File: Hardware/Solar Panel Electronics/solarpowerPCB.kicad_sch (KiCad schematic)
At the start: 41 parts, among them J3 Conn_01x02_Male, J4 Conn_01x06_Male, J5 Conn_01x02_Male, Q1 MMDT2222A, U1 SN65HVD230, U2 ESP32-PICO-D4

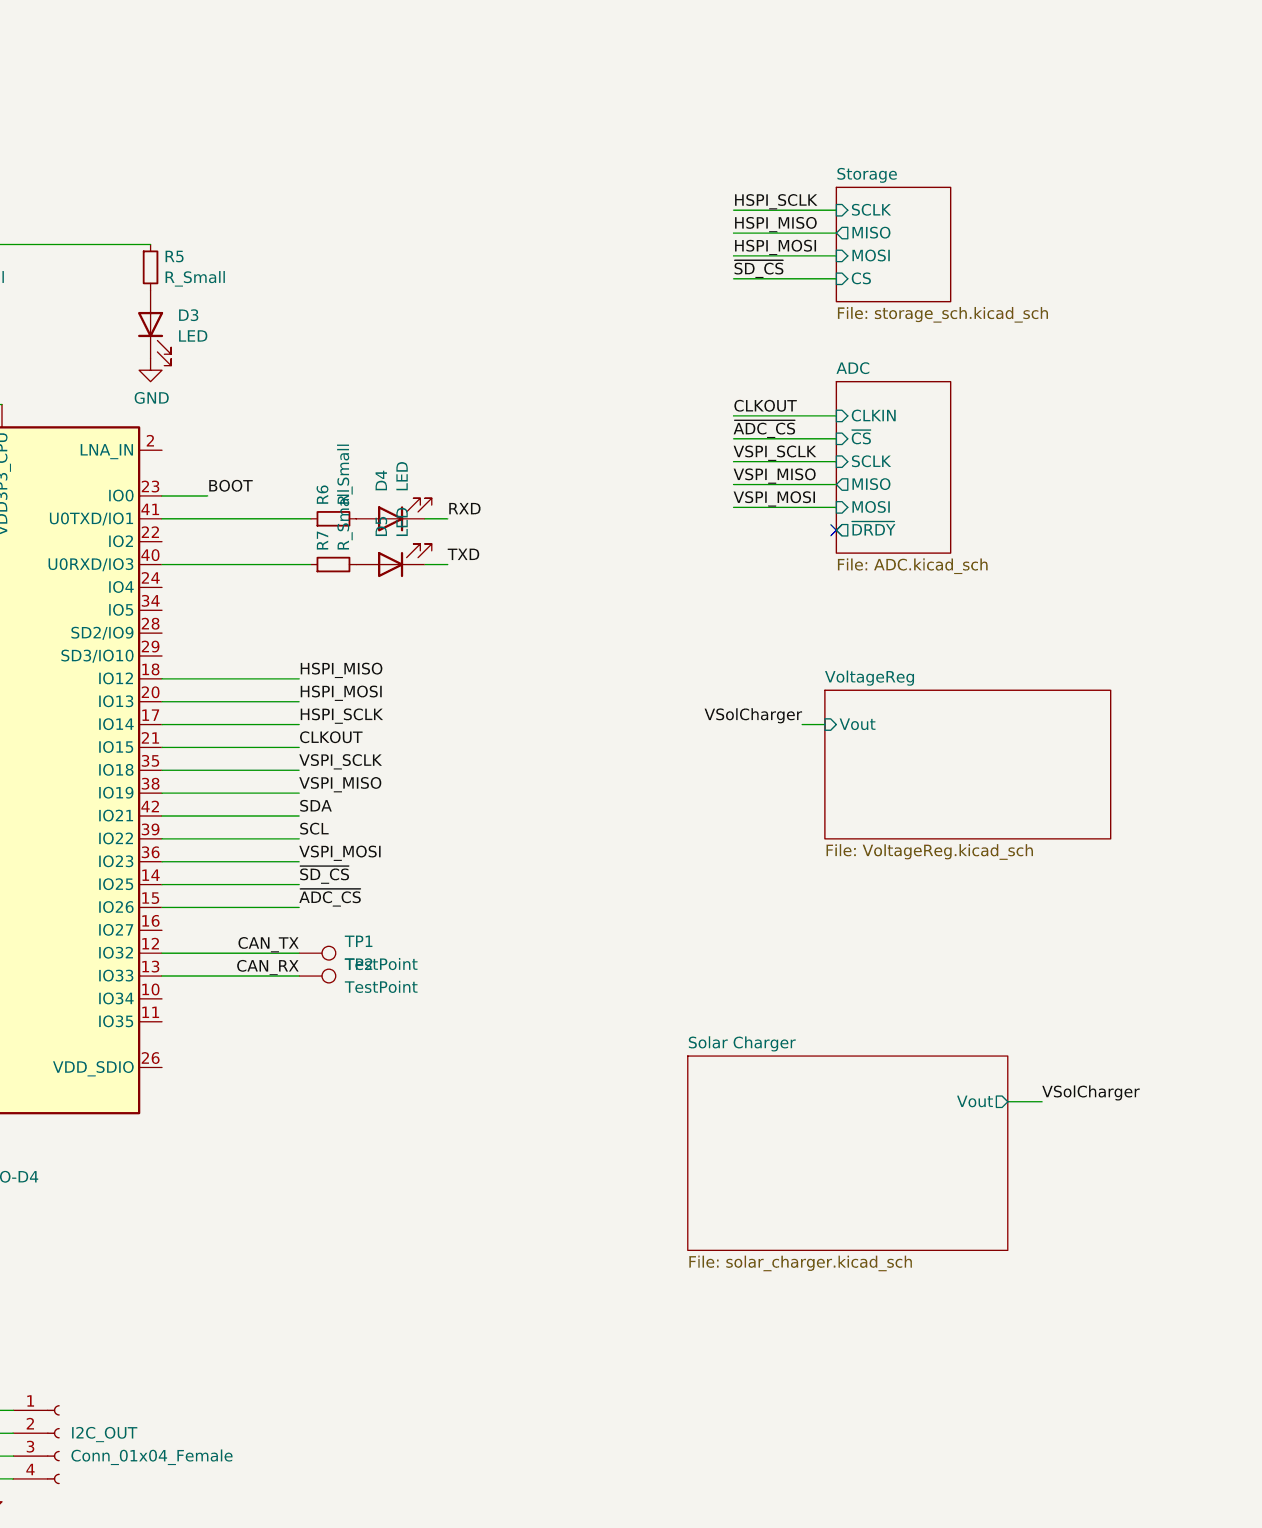
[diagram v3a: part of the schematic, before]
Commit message: Added power measuring circuitry using potential dividers. Needs to be double checked
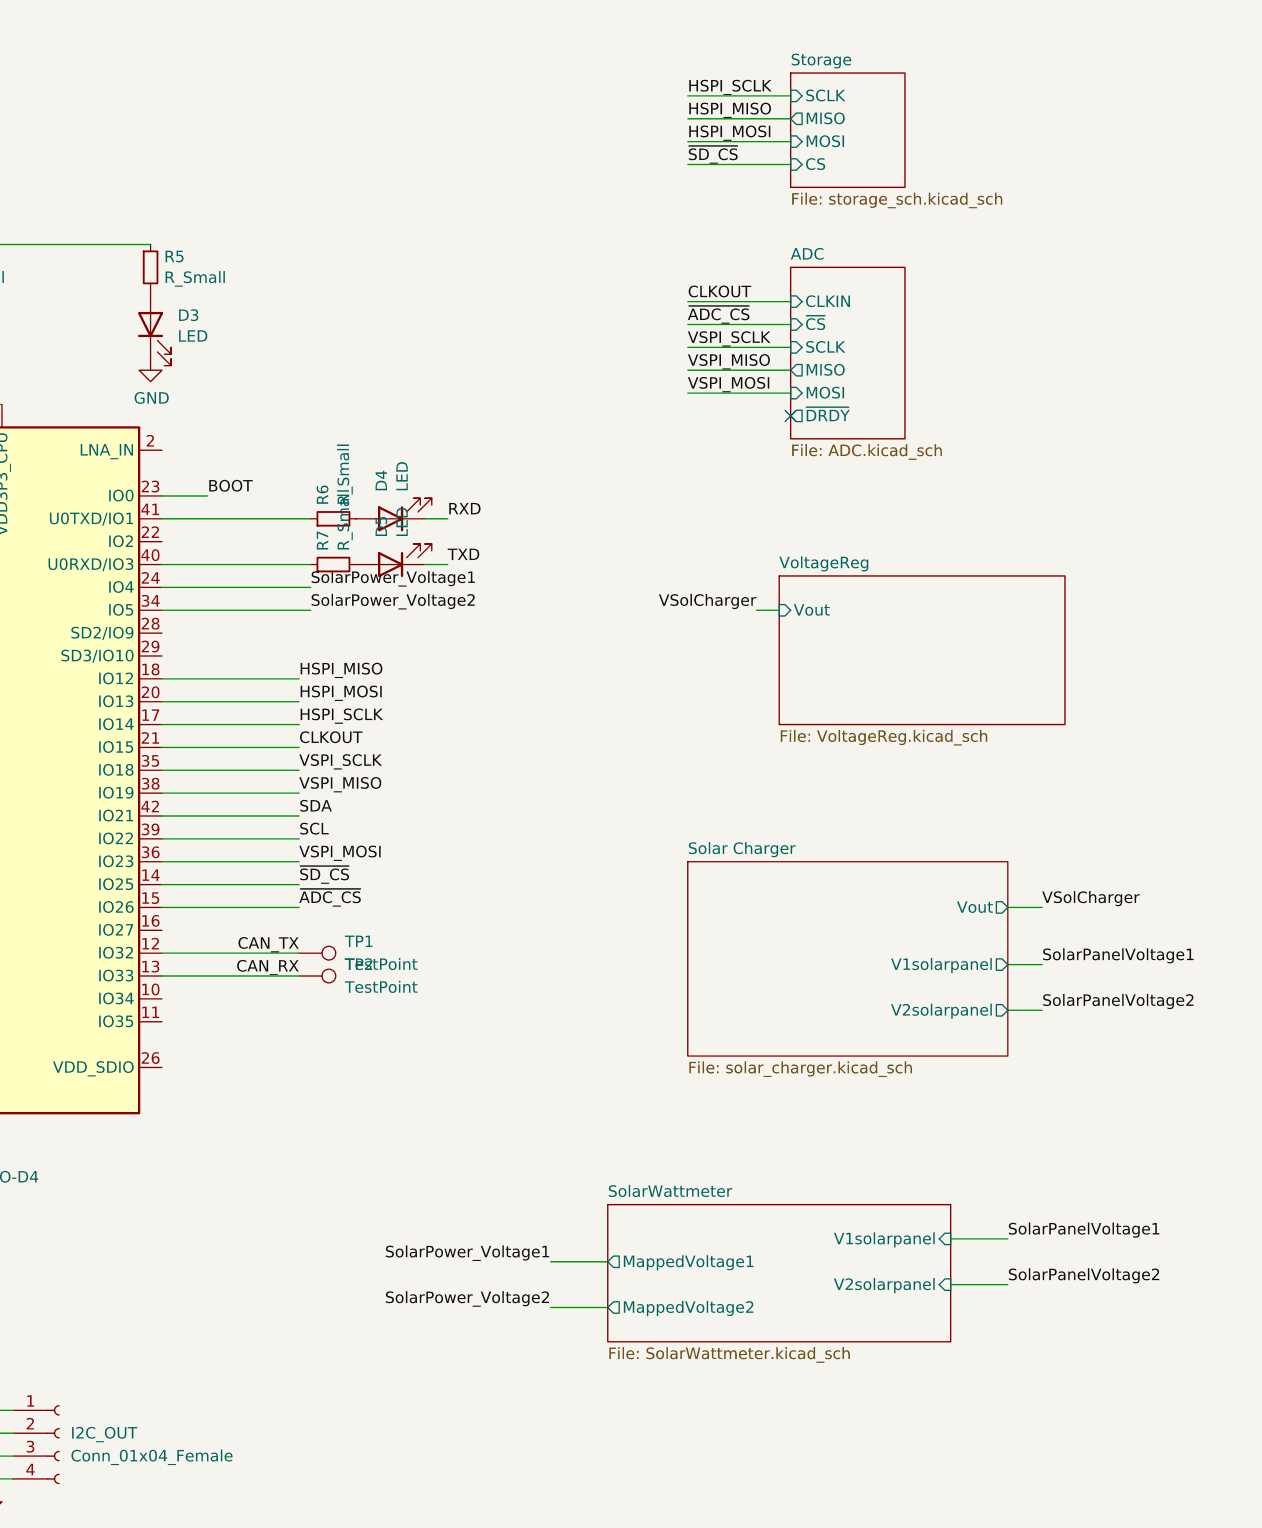
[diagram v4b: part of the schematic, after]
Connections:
- net SolarPower_Voltage1: now reaches U2.24 (IO4)
- net SolarPower_Voltage2: now reaches U2.34 (IO5)
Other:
- added sheet SolarWattmeter (SolarWattmeter.kicad_sch)
- sheet Solar Charger ports: added V1solarpanel, V2solarpanel; removed none

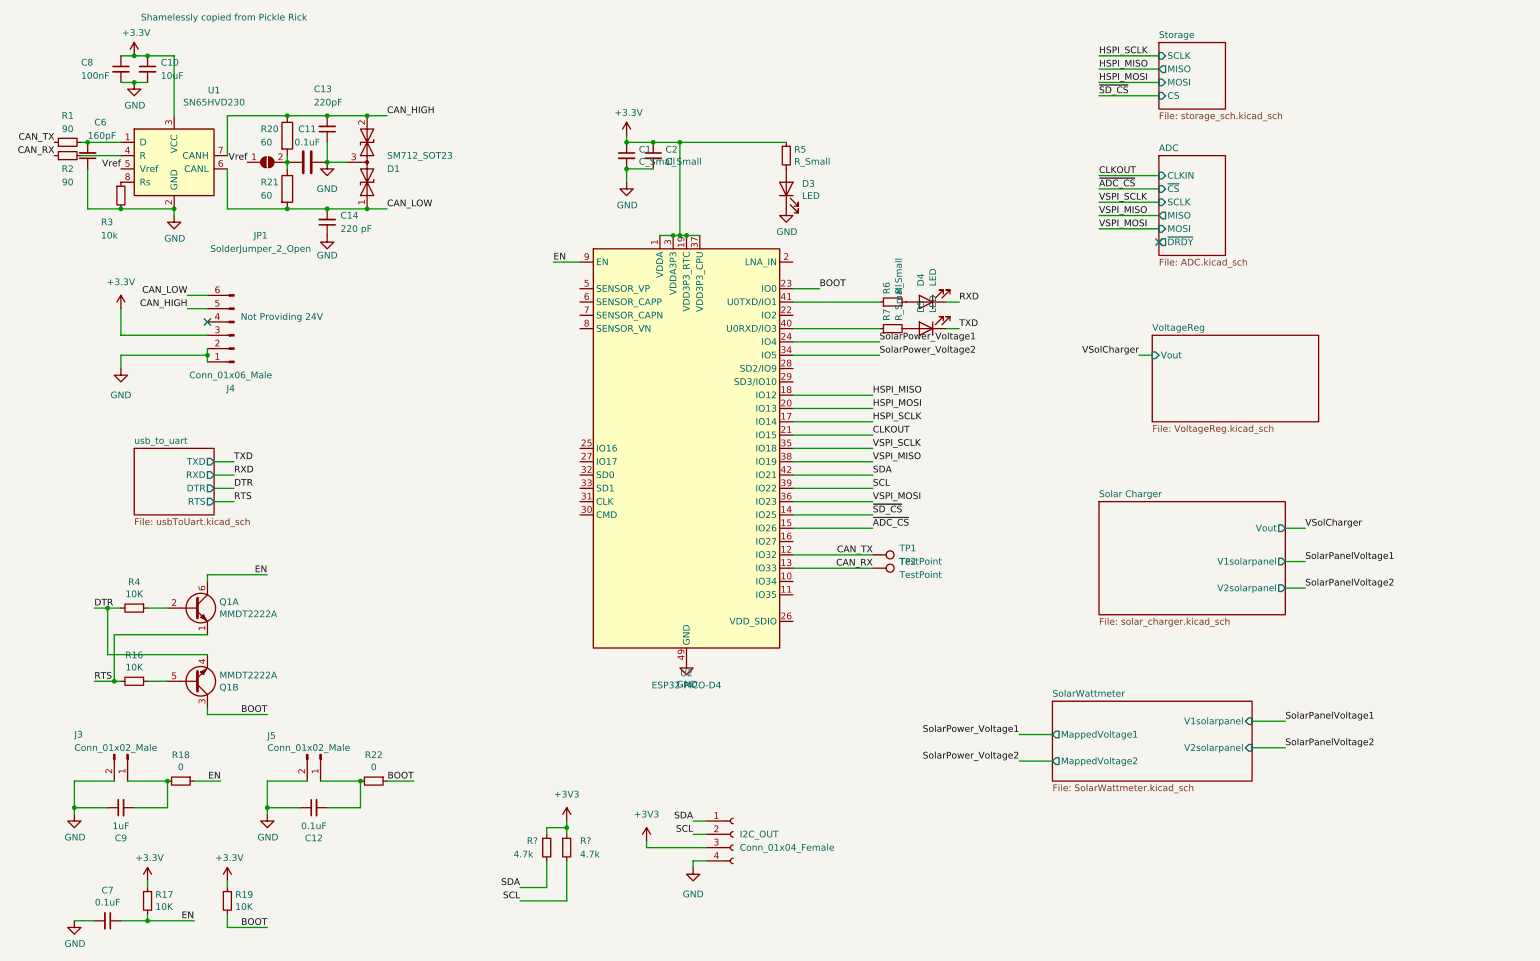
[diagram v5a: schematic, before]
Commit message: Changed to use ADS131M04 adc instead of esp32 adc for power calculation
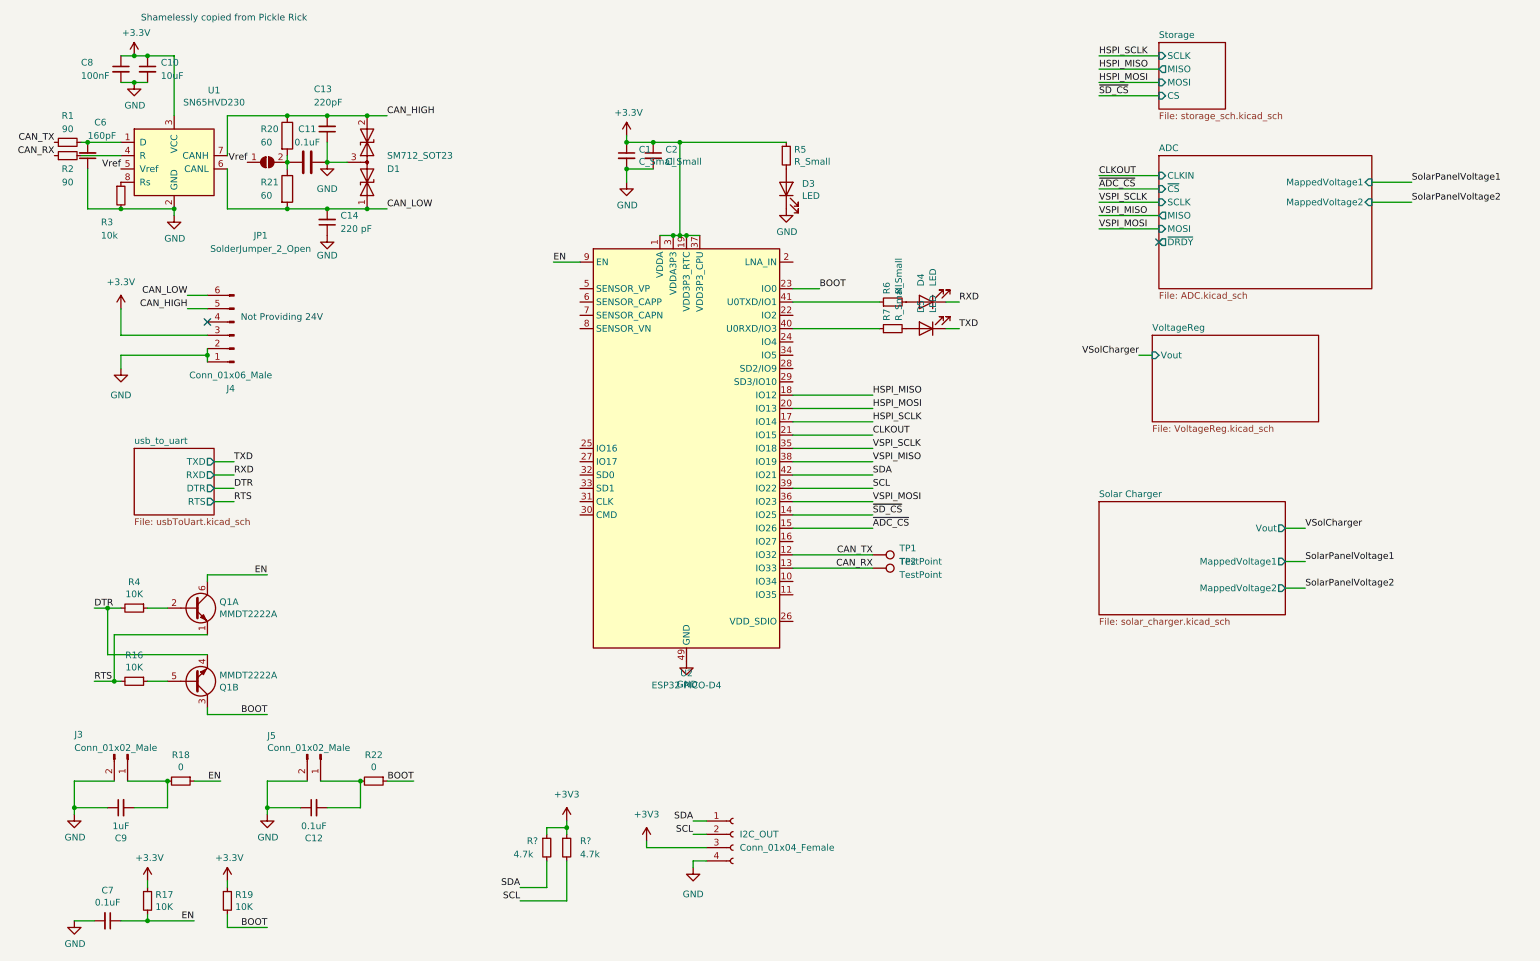
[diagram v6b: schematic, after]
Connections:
- net SolarPower_Voltage1: no longer names the net of U2.24 (IO4)
- net SolarPower_Voltage2: no longer names the net of U2.34 (IO5)
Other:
- removed sheet SolarWattmeter
- sheet ADC ports: added MappedVoltage1, MappedVoltage2; removed none
- sheet Solar Charger ports: added MappedVoltage1, MappedVoltage2; removed V1solarpanel, V2solarpanel

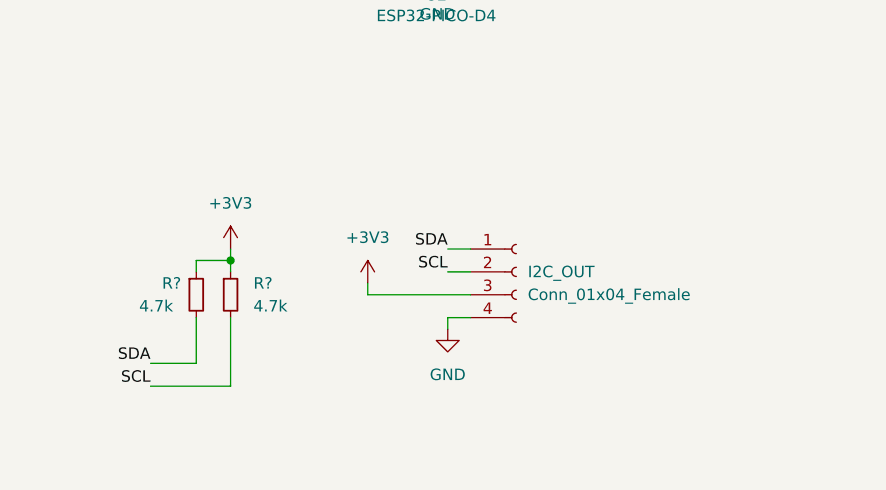
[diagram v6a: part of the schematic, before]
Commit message: Assigned Footprints (preliminary - just to do a quick layout)
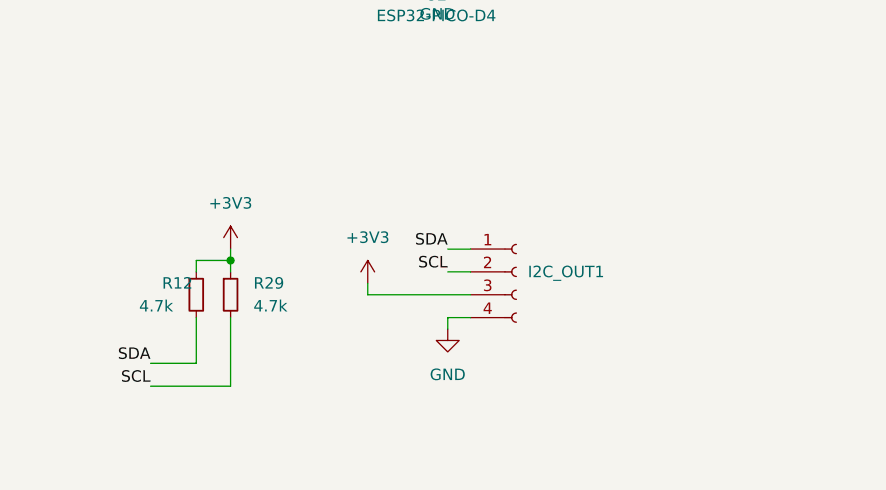
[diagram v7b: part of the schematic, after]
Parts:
- I2C_OUT1: renamed from I2C_OUT; value Conn_01x04_Female -> (none)
- gave numbers to parts that had none: 2
